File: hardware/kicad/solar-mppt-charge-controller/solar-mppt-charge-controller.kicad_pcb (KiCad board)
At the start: 2 copper layers, 99 x 60 mm, 21 parts, among them J1 SOLAR_IN, J2 LOAD_OUT, J3 ESP32_DEVKIT, J4 DEBUG_UART, U1 LM2596S-ADJ, U2 MCP4131-103, U3 INA226xA, U4 INA226xB

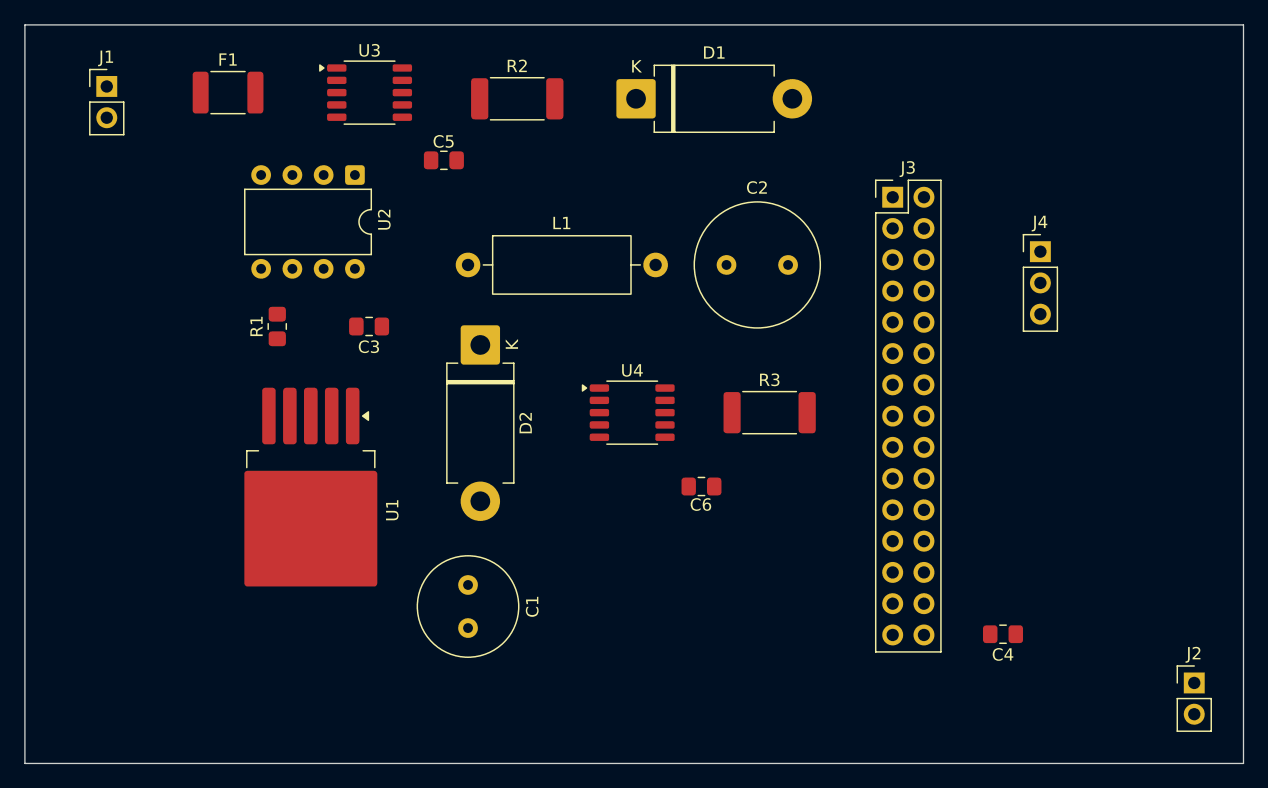
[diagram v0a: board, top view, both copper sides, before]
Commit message: PCB: routing complete, GND vias and F1 net issue remaining
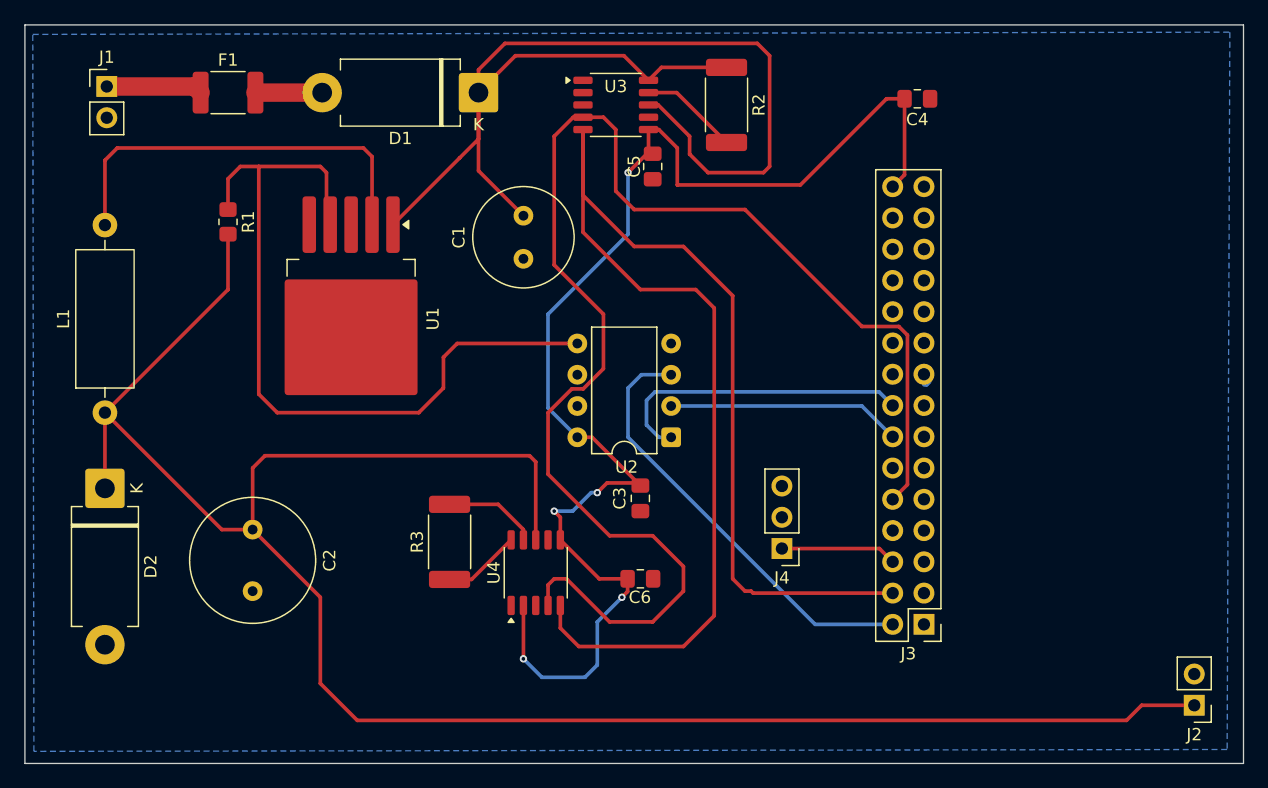
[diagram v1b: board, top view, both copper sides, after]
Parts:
- moved C2 44.1 mm to (125.5, 105.0), turned to -90 degrees
- moved C4 44.1 mm to (179.5, 70.0)
- moved J3 34.8 mm to (180.0, 112.7), turned to 180 degrees
- moved U2 33.4 mm to (159.5, 97.5), turned to 180 degrees
- moved D2 32.6 mm to (113.5, 101.7)
- moved J4 32.0 mm to (168.5, 106.5), turned to 180 degrees
- moved L1 31.8 mm to (113.5, 95.5), turned to 90 degrees
- moved R3 28.0 mm to (141.5, 106.0), turned to 90 degrees
- moved C1 26.9 mm to (147.5, 83.0), turned to 90 degrees
- moved C3 26.1 mm to (157.0, 102.5), turned to 90 degrees
- moved U3 20.0 mm to (155.0, 70.5)
- moved R2 17.0 mm to (164.0, 70.5), turned to -90 degrees
- moved C5 17.0 mm to (158.0, 75.5), turned to 90 degrees
- moved U1 15.9 mm to (133.5, 87.9)
- moved U4 15.2 mm to (148.5, 108.5), turned to 90 degrees
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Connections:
- C1 pad 1: (no net) -> GND
- C1 pad 2: (no net) -> /PANEL_IN
- C2 pad 1: (no net) -> /VOUT
- C3 pad 2: (no net) -> +3.3V
- D1 pad 2: (no net) -> /FUSE_OUT
- F1 pad 1: Net-(D1-A) -> /FUSE_OUT
- F1 pad 2: Net-(D1-A) -> /FUSE_OUT
- J1 pad 1: Net-(D1-A) -> /FUSE_OUT
- J3 pad 1: (no net) -> unconnected-(J3-Pin_1-Pad1)
- J3 pad 10: (no net) -> /I2C_SDA
- J3 pad 11: (no net) -> unconnected-(J3-Pin_11-Pad11)
- J3 pad 12: (no net) -> unconnected-(J3-Pin_12-Pad12)
- J3 pad 13: (no net) -> unconnected-(J3-Pin_13-Pad13)
- J3 pad 14: (no net) -> /SPI_SCK
- J3 pad 15: (no net) -> unconnected-(J3-Pin_15-Pad15)
- J3 pad 16: (no net) -> /SPI_CS
- J3 pad 17: (no net) -> unconnected-(J3-Pin_17-Pad17)
- J3 pad 18: (no net) -> unconnected-(J3-Pin_18-Pad18)
- J3 pad 19: (no net) -> unconnected-(J3-Pin_19-Pad19)
- J3 pad 2: (no net) -> /SPI_MOSI
- J3 pad 20: (no net) -> unconnected-(J3-Pin_20-Pad20)
- J3 pad 21: (no net) -> unconnected-(J3-Pin_21-Pad21)
- J3 pad 22: (no net) -> unconnected-(J3-Pin_22-Pad22)
- J3 pad 23: (no net) -> unconnected-(J3-Pin_23-Pad23)
- J3 pad 24: (no net) -> unconnected-(J3-Pin_24-Pad24)
- J3 pad 25: (no net) -> unconnected-(J3-Pin_25-Pad25)
- J3 pad 26: (no net) -> unconnected-(J3-Pin_26-Pad26)
- J3 pad 27: (no net) -> unconnected-(J3-Pin_27-Pad27)
- J3 pad 4: (no net) -> /I2C_SCL
- J3 pad 5: (no net) -> unconnected-(J3-Pin_5-Pad5)
- J3 pad 6: (no net) -> /UART_TX
- J3 pad 7: (no net) -> unconnected-(J3-Pin_7-Pad7)
- J3 pad 8: (no net) -> unconnected-(J3-Pin_8-Pad8)
- J3 pad 9: (no net) -> unconnected-(J3-Pin_9-Pad9)
- J4 pad 2: (no net) -> unconnected-(J4-Pin_2-Pad2)
- L1 pad 2: (no net) -> Net-(U1-OUT)
- R1 pad 1: (no net) -> /FB_DIV
- R2 pad 2: (no net) -> /PANEL_SENSE
- R3 pad 2: (no net) -> /LOAD_SENSE
- U2 pad 7: (no net) -> unconnected-(U2-P0B-Pad7)
- U3 pad 3: (no net) -> unconnected-(U3-~{Alert}-Pad3)
- U4 pad 3: (no net) -> unconnected-(U4-~{Alert}-Pad3)
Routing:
- net /VOUT: track 0.00 -> 169.5 mm
- net /I2C_SCL: track 0.00 -> 119.9 mm
- net /I2C_SDA: track 0.00 -> 116.4 mm
- net +3.3V: track 0.00 -> 108.3 mm, vias 0 -> 5
- net /PANEL_IN: track 0.00 -> 98.9 mm
- net /FB_DIV: track 0.00 -> 64.3 mm
- net /SPI_MOSI: track 0.00 -> 35.7 mm
- net Net-(U1-OUT): track 0.00 -> 33.2 mm
- net /SPI_CS: track 0.00 -> 25.2 mm
- net /SPI_SCK: track 0.00 -> 19.0 mm
- net /FUSE_OUT: track 0.00 -> 13.3 mm
- net /UART_TX: track 0.00 -> 9.45 mm
- net /PANEL_SENSE: track 0.00 -> 8.02 mm
- net /LOAD_SENSE: track 0.00 -> 7.69 mm
- net unconnected-(J3-Pin_17-Pad17): track 0.00 -> 0.56 mm
- added copper zone on B.Cu, net GND
